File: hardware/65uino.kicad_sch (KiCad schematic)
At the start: 46 parts, among them J1 Barrel_Jack_MountingPin, J2 USB_B_Micro, J3 OLED, SW1 RST, SW2 BTN, U1 R6507, U2 74HC04, U3 6532, U4 w27C512, U5 MIC5504-3.3YM5, U6 LM1117-5.0, X1 NC, Y1 1Mhz

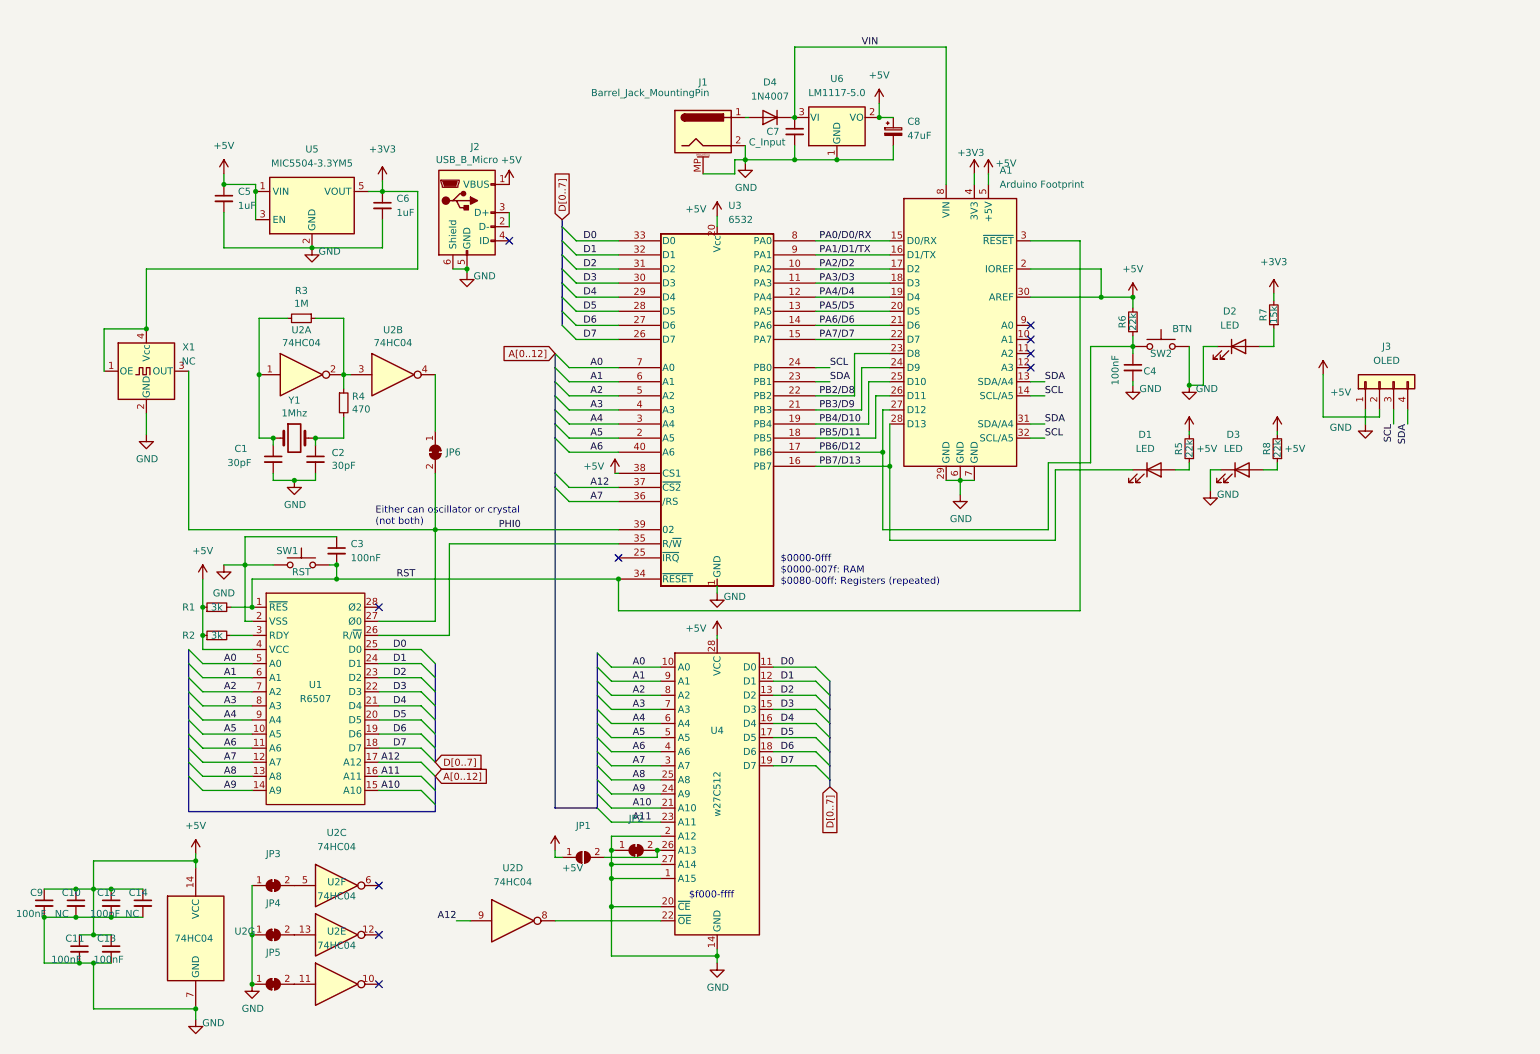
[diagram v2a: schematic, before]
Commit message: Pullups on serial and i2c lines + Single gate sot23-5 inverter default
Added some "optional" pullups on the serial lines and i2c lines. Default is now to use a 1 gate sot23-5 inverter for address decoding instead of the DIP14 inverter, as well as the SMD oscillator instead of the inverter crystal oscillator circuit.
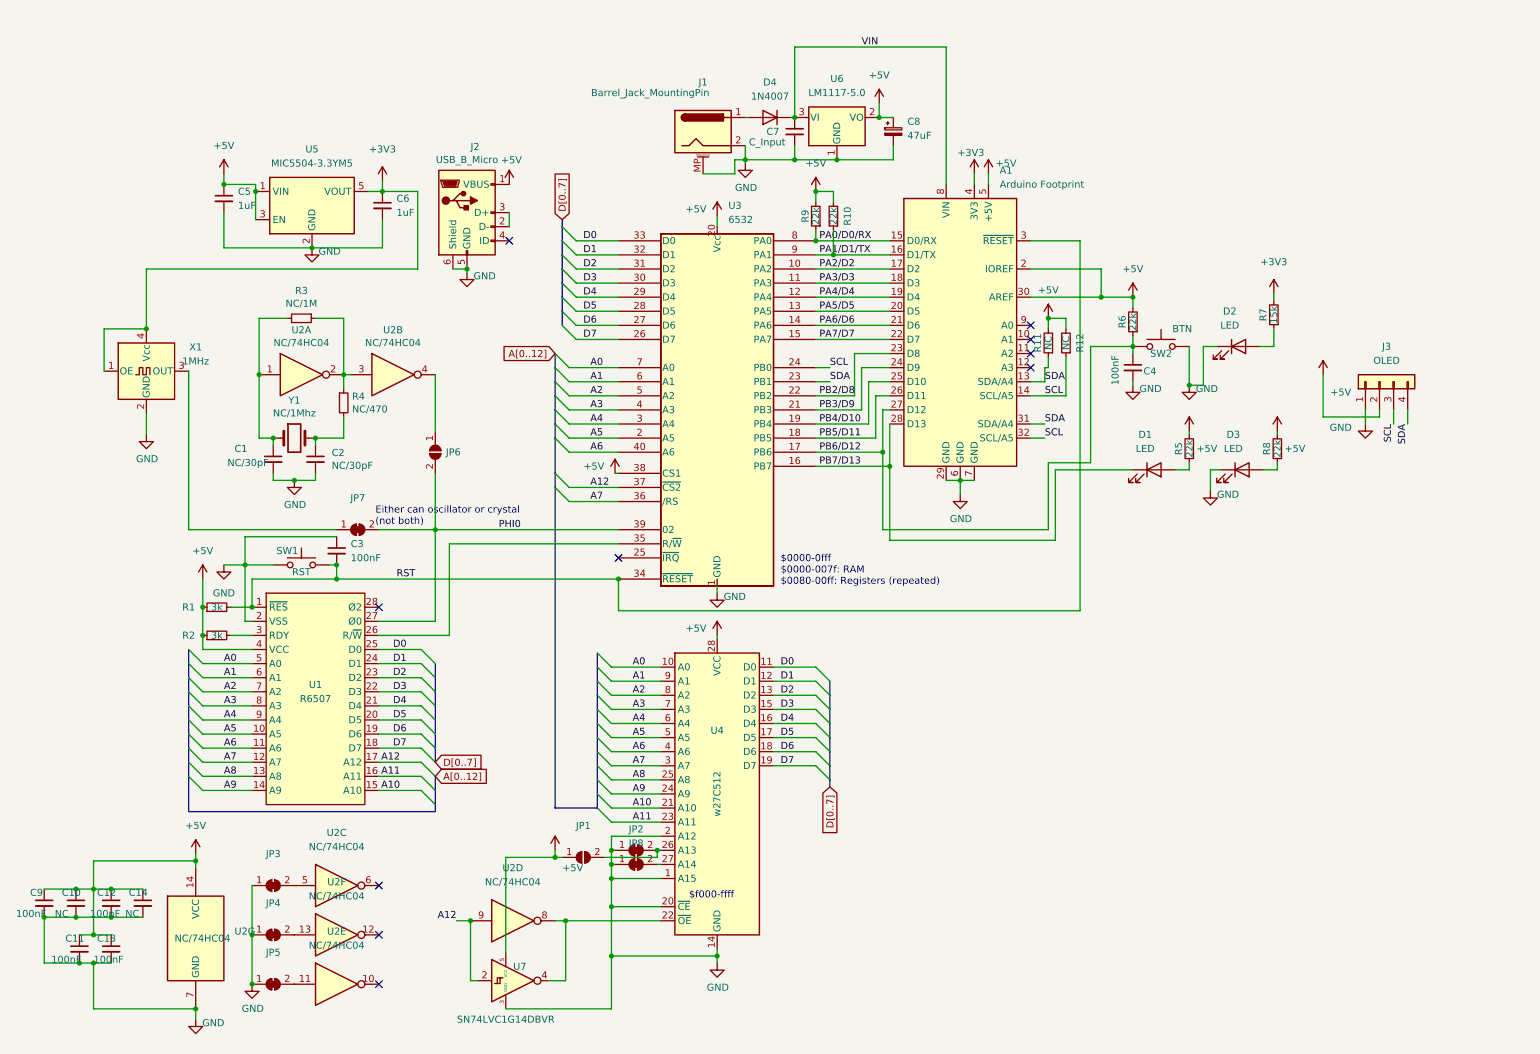
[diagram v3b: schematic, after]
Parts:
- added JP7, JP8: SolderJumper_2_Bridged, Jumper:SolderJumper-2_P1.3mm_Bridged_RoundedPad1.0x1.5mm, symbol Jumper:SolderJumper_2_Bridged
- added R10, R9: 22k, Resistor_SMD:R_0805_2012Metric, symbol Device:R_Small
- added R11, R12: NC, Resistor_SMD:R_0805_2012Metric, symbol Device:R_Small
- added U7: SN74LVC1G14DBVR, Package_TO_SOT_SMD:SOT-23-5, symbol 74xGxx:SN74LVC1G14DBV
- C1, C2: value 30pF -> NC/30pF
- JP6: footprint Jumper:SolderJumper-2_P1.3mm_Bridged_RoundedPad1.0x1.5mm -> Jumper:SolderJumper-2_P1.3mm_Open_RoundedPad1.0x1.5mm; symbol Jumper:SolderJumper_2_Bridged -> Jumper:SolderJumper_2_Open
- R3: value 1M -> NC/1M
- R4: value 470 -> NC/470
- U2: value 74HC04 -> NC/74HC04
- X1: value NC -> 1MHz
- Y1: value 1Mhz -> NC/1Mhz
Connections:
- net +5V: now also R10.2, R11.2, R12.2, R9.2, U7.5 (VCC)
- net A12: now also U7.2
- net GND: now also JP8.1 (A), U7.3 (GND); no longer U4.27 (A14)
- net PA0/D0/RX: now also R9.1
- net PA1/D1/TX: now also R10.1
- net PHI0: now also JP7.2 (B); no longer X1.3 (OUT)
- net SCL: now also R12.1
- net SDA: now also R11.1
- net at U2.8, U4.22 (~{OE}): now also U7.4
- new net: JP7.1 (A), X1.3 (OUT)
- new net: JP8.2 (B), U4.27 (A14)

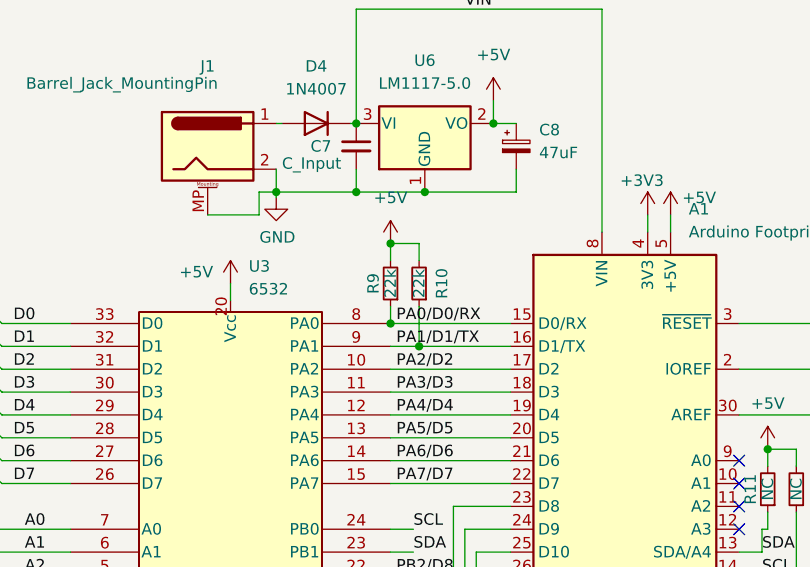
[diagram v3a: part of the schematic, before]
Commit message: Better SSD1306 lib, automatic bootloading and more
Better SSD1306 lib - Now does CR/NL + backspace
Automatic bootloading
Speed optimizations
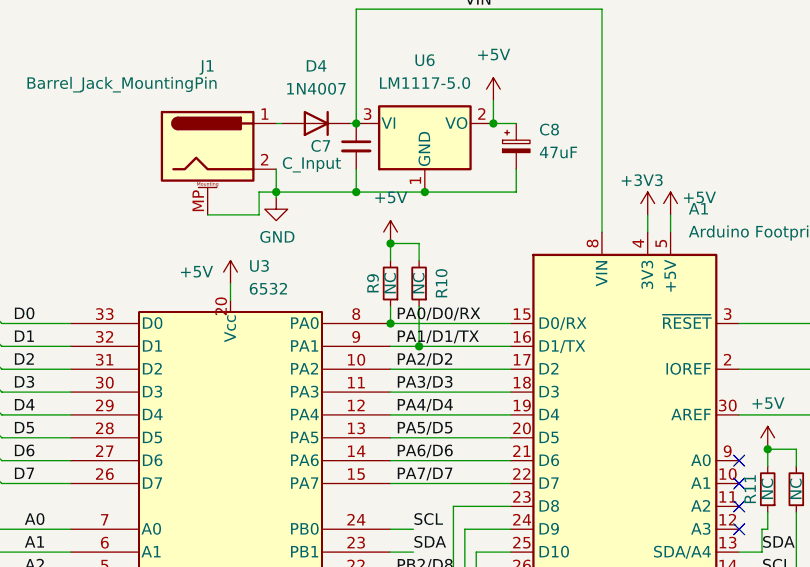
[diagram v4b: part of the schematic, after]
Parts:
- R10, R9: value 22k -> NC
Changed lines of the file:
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@@
     (in_bom yes) (on_board yes)
     (property "Reference" "R10" (id 0) (at 161.925 48.895 90))
-    (property "Value" "22k" (id 1) (at 159.385 48.895 90))
+    (property "Value" "NC" (id 1) (at 159.385 48.895 90))
     (property "Footprint" "Resistor_SMD:R_0805_2012Metric" (id 2) (at 159.385 48.895 0)
       (effects (font (size 1.27 1.27)) hide)
@@
     (in_bom yes) (on_board yes)
     (property "Reference" "R9" (id 0) (at 154.305 48.895 90))
-    (property "Value" "22k" (id 1) (at 156.21 48.895 90))
+    (property "Value" "NC" (id 1) (at 156.21 48.895 90))
     (property "Footprint" "Resistor_SMD:R_0805_2012Metric" (id 2) (at 156.21 48.895 0)
       (effects (font (size 1.27 1.27)) hide)
@@
     )
     (path "/dfad4f63-1329-4133-8e1c-a2b5603859c8"
-      (reference "R9") (unit 1) (value "22k") (footprint "Resistor_SMD:R_0805_2012Metric")
+      (reference "R9") (unit 1) (value "NC") (footprint "Resistor_SMD:R_0805_2012Metric")
     )
     (path "/a0b12754-363c-4de9-9292-e49765088392"
-      (reference "R10") (unit 1) (value "22k") (footprint "Resistor_SMD:R_0805_2012Metric")
+      (reference "R10") (unit 1) (value "NC") (footprint "Resistor_SMD:R_0805_2012Metric")
     )
     (path "/eb32f0f6-14a8-4a9d-a571-fd7b94f6f48e"

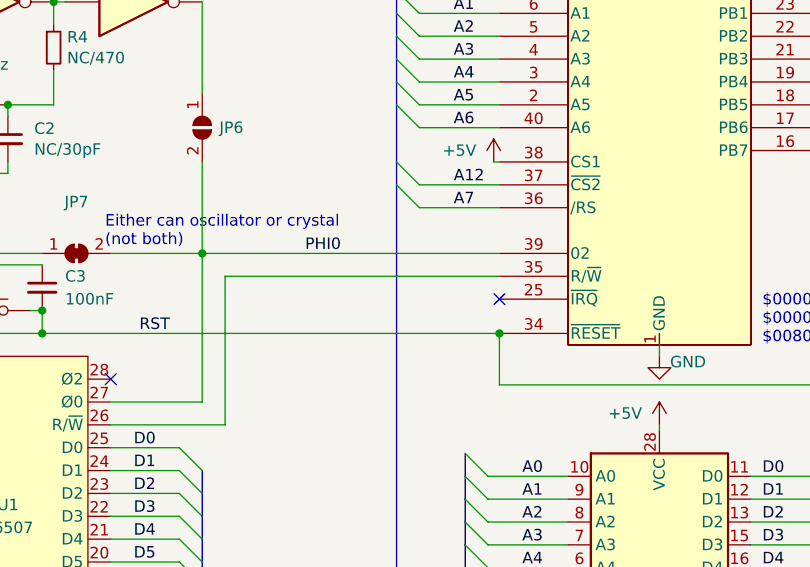
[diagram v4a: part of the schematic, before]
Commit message: Gerbers updated to match KiCAD
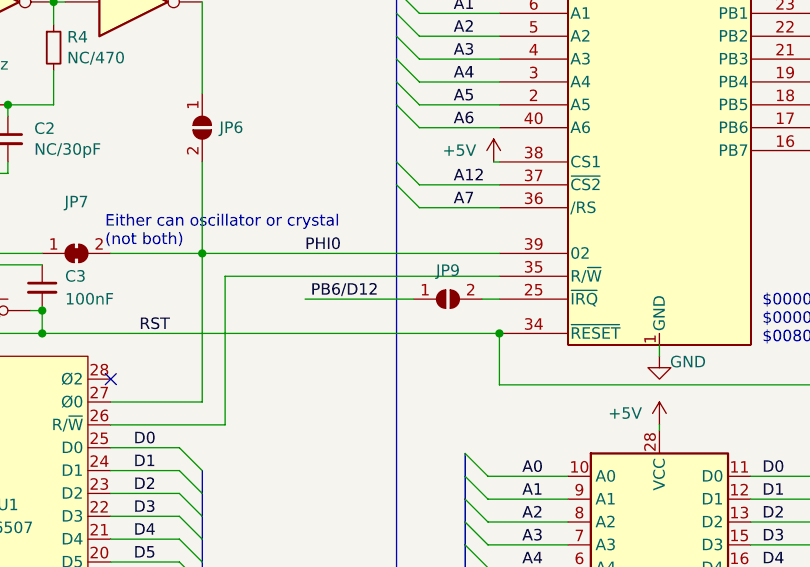
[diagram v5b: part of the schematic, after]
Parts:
- added JP9: SolderJumper_2_Bridged, Jumper:SolderJumper-2_P1.3mm_Open_RoundedPad1.0x1.5mm, symbol Jumper:SolderJumper_2_Open
- D4: footprint Diode_SMD:D_SMB_Handsoldering -> Diode_SMD:D_SMB
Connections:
- net PB6/D12: now also JP9.1 (A)
- net at U3.25 (~{IRQ}): now also JP9.2 (B)
- no-connect marks 10 -> 9
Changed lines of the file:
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@@
   (no_connect (at 194.945 73.66))
   (no_connect (at 194.945 76.2))
-  (no_connect (at 120.65 110.49))
   (no_connect (at 100.965 53.34))
   (no_connect (at 77.47 119.38))
@@
     (stroke (width 0) (type default) (color 0 0 0 0))
   )
+  (wire (pts (xy 99.06 110.49) (xy 111.125 110.49))
+    (stroke (width 0) (type default) (color 0 0 0 0))
+  )
   (bus (pts (xy 116.84 145.415) (xy 116.84 147.955))
     (stroke (width 0) (type default) (color 0 0 0 0))
@@
     (stroke (width 0) (type default) (color 0 0 0 0))
   )
+  (wire (pts (xy 118.745 110.49) (xy 120.65 110.49))
+    (stroke (width 0) (type default) (color 0 0 0 0))
+  )
   (wire (pts (xy 213.36 78.74) (xy 213.36 79.375))
     (stroke (width 0) (type default) (color 0 0 0 0))
@@
     (effects (font (size 1.27 1.27)) (justify left bottom))
   )
+  (label "PB6{slash}D12" (at 99.695 110.49 0)
+    (effects (font (size 1.27 1.27)) (justify left bottom))
+  )
   (label "A0" (at 123.19 130.175 0)
     (effects (font (size 1.27 1.27)) (justify left bottom))
@@
     (property "Reference" "D4" (id 0) (at 147.955 24.765 0))
     (property "Value" "1N4007" (id 1) (at 147.955 27.305 0))
-    (property "Footprint" "Diode_SMD:D_SMB_Handsoldering" (id 2) (at 147.955 26.67 0)
+    (property "Footprint" "Diode_SMD:D_SMB" (id 2) (at 147.955 26.67 0)
       (effects (font (size 1.27 1.27)) hide)
     )
@@
     (pin "2")
   )
+  (symbol (lib_id "Jumper:SolderJumper_2_Open") (at 114.935 110.49 0) (unit 1)
+    (in_bom yes) (on_board yes) (fields_autoplaced)
+    (property "Reference" "JP9" (id 0) (at 114.935 107.315 0))
+    (property "Value" "SolderJumper_2_Bridged" (id 1) (at 114.935 107.315 0)
+      (effects (font (size 1.27 1.27)) hide)
+    )
+    (property "Footprint" "Jumper:SolderJumper-2_P1.3mm_Open_RoundedPad1.0x1.5mm" (id 2) (at 114.935 110.49 0)
+      (effects (font (size 1.27 1.27)) hide)
+    )
+    (property "Datasheet" "~" (id 3) (at 114.935 110.49 0)
+      (effects (font (size 1.27 1.27)) hide)
+    )
+    (pin "1")
+    (pin "2")
+  )
   (symbol (lib_id "power:GND") (at 213.36 79.375 0) (unit 1)
     (in_bom yes) (on_board yes)
@@
     )
     (path "/b2f2bb30-d859-4087-9deb-61e21f866a12"
-      (reference "D4") (unit 1) (value "1N4007") (footprint "Diode_SMD:D_SMB_Handsoldering")
+      (reference "D4") (unit 1) (value "1N4007") (footprint "Diode_SMD:D_SMB")
     )
     (path "/6f6c4507-8d30-4097-87ba-ba3063b0cd50"
@@
       (reference "JP8") (unit 1) (value "SolderJumper_2_Bridged") (footprint "Jumper:SolderJumper-2_P1.3mm_Bridged_RoundedPad1.0x1.5mm")
     )
+    (path "/b3a91383-4c83-4a9b-a912-a82c484cd5d3"
+      (reference "JP9") (unit 1) (value "SolderJumper_2_Bridged") (footprint "Jumper:SolderJumper-2_P1.3mm_Open_RoundedPad1.0x1.5mm")
+    )
     (path "/3ef5b4e1-29cb-458d-b968-1b8688bc08b3"
